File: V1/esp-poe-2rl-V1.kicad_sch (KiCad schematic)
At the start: 91 parts, among them J1 USB_C_Receptacle_USB2.0, J2 RJ45 JACK, J3 Conn_01x02, J4 Conn_01x02, K1 Relay 5V 15A, K2 Relay 5V 15A, Q1 WPM2015-3/TR, Q2 LMUN2211LT1G, Q3 UMH3N, Q4 MMBT2222A, Q5 MMBT2222A, SW1 RESET, U1 TPS2376D, U2 TX4138, U3 SY8089A1AAC, U4 CH340C, U5 ESP32-WROOM-32UE-N16, U6 LAN8710A

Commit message: Dev dev dev
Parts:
- J2: footprint Tales:RJ45_UDE_RB1-ZZ-0266 -> Tales:RJ45_UDE_RB1-ZZ-0206
- U1: value TPS2376D -> TPS2376DDAR-H
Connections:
- net +3.3VA: now also J2.12 (RLED+); no longer J2.L2 (RLED+)
- net LED_Y_A: now also J2.14 (LLED+); no longer J2.L4 (LLED+)
- net at R27.1: now also J2.13 (LLED-); no longer J2.L3 (LLED-)
- net at R28.1: now also J2.11 (RLED-); no longer J2.L1 (RLED-)
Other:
- note added: "OPÇÕES RJ45 UDE CORP RB1-ZZ-0266 JLCPCB C409617 HCTL HC931147C-M897-A JLCPCB C3021372 HANRUN HY931147C JLCPCB C91754 ABRACON ARJP11A-MASA-B-A-FMU2 MOUSER 815-ARJP11AMAFMU2 CUI DEVICES CRJ005-M1-TH MOUSER 490-CRJ005-M1-TH SEM LEDS SEM DIODOS MDD MB6S JLCPCB C2487 PONTE RETIFICADORA"
- note added: "R_{DIV1}"
- note added: "R_{DIV2}"
- note added: "V_{TAP} MUST BE 2.5V WHEN VDD IS AT THE DESIRED TURN ON VOLTAGE. V_{TAP} = V_{DD} * R_{DIV2} / (R_{DIV1}+R_{DIV2}) 2.5 = V_{DD} * 31.6 / 443.6 V_{DD} = 35.1V -> OK THE TOTAL RESISTANCE OF THE VOLTAGE DIVIDER WILL APPEAR IN PARALLEL WITH R_{DET} TO FORM THE EQUIVALENT RESISTANCE AT PIN DET. R_{EQUIV} = (R_{DIV1} + R_{DIV2}) // R_{DET} R_{EQUIV} = 443.6 // 26.7 R_{EQUIV} = 25.184k -> OK"
- note removed: "UDE CORP RB1-ZZ-0266 JLC C409617 1,24 ABRACON MOUSER 815-ARJP11AMAFMU2 9,05 CUI DEVICES MOUSER 490-CRJ005-M1-TH 5,67 NÃO TEM DIODOS INTERNOS JLCPCB C114100 MOLEX 424108312 JLCPCB C508567 JLCPCB C305935"
- note removed: "V_{TAP} MUST BE 2.5V WHEN VDD IS AT THE DESIRED TURN ON VOLTAGE. V_{TAP} = V_{DD} * R_{2} / (R_{1}+R_{2}) 2.5 = V_{DD} * 31.6 / 443.6 V_{DD} = 35.1V -> OK THE TOTAL RESISTANCE OF THE VOLTAGE DIVIDER (R_{1} + R_{2}) WILL APPEAR IN PARALLEL WITH R_{DET} TO FORM THE EQUIVALENT RESISTANCE AT PIN DET. R_{EQUIV} = (R_{1} + R_{2}) // R_{DET} R_{EQUIV} = 443.6 // 26.7 R_{EQUIV} = 25.184k -> OK"
- moved on the sheet: C2, R27, R28, R7

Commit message: dev goes on
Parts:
- R1: value 412k/62,5mW -> 130k/62,5mW; LCSC Part # C187991 -> C93946; Mfr TA-I Tech -> YAGEO; Mfr PN RM04FTN4123 -> RC0402FR-07130KL; Vendor PN C187991 -> C93946
- R13, R18, R19, R20, R21, R29, R32: LCSC Part # C25744 -> C60490; Mfr Uniroyal -> YAGEO; Mfr PN 0402WGF1002TCE -> RC0402FR-0710KL; Technology (none) -> 1%; Vendor PN C25744 -> C60490
- R2: value 31.6k/62,5mW -> 10k/62,5mW; LCSC Part # C100371 -> C60490; Mfr LIZ Elec -> YAGEO; Mfr PN CR0402FF3162G -> RC0402FR-0710KL; Vendor PN C100371 -> C60490
- R3: LCSC Part # C965284 -> C138046; Mfr Uniroyal -> YAGEO; Mfr PN NQ02WGF1803TCE -> RC0402FR-07180KL; Vendor PN C965284 -> C138046
- R4: value 4,42k/62,5mW -> 4,42k/100mW; footprint Tales:R_0402_1005Metric -> Tales:R_0603_1608Metric; Case 0402/1005 -> 0603/1608; LCSC Part # C173614 -> C482858; Mfr HKR -> YAGEO; Mfr PN RCT024K42FLF -> RC0603FR-074K42L; Vendor PN C173614 -> C482858
- R5: value 26,7k/62,5mW -> 30,1k/62,5mW; LCSC Part # C304992 -> C226982; Mfr Ralec -> YAGEO; Mfr PN RTT022672DTH -> AC0402FR-0730K1L; Technology 0,5% -> 1%; Vendor PN C304992 -> C226982
- R6: value 30mR/0,250W -> 30mR/250mW; LCSC Part # C247605 -> C859791; Mfr Uniroyal -> YAGEO; Mfr PN 0805W4F300MT5E -> RL0805FR-7W0R03L; Vendor PN C247605 -> C859791
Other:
- note added: "453/31.6 475/32.4 -> 26.1 178/12.1 -> 28.7"
- note added: "TPS2375 (IEEE 802.3af) TURN ON VOLTAGE = 39.3V TURN OFF VOLTAGE = 30.5V TPS2376-H TURN ON VOLTAGE: V_{TAP} = 2.49V HYSTERESIS = 0.56V TURN OFF VOLTAGE: V_{TAP} = 1.93V. V_{TAP} = V_{DD} * R_{DIV2} / (R_{DIV1}+R_{DIV2}) TURN ON: 2.5 = V_{DD} * 31.6 / 443.6 V_{DD} = 35.09V -> OK TURN 0FF: 1.93 = V_{DD} * 31.6 / 443.6 V_{DD} = 27.09V -> OK"
- note added: "VALUE FOR THE DETECTION RESISTANCE MUST BE 24.9K +/- 1% OR 24,651K TO 25.149K. THE TOTAL RESISTANCE OF THE VOLTAGE DIVIDER TO UVLO WILL APPEAR IN PARALLEL WITH R_{DET} TO FORM THE EQUIVALENT DETECTION RESISTANCE. R_{EQUIV} = (R_{DIV1} + R_{DIV2}) // R_{DET} R_{EQUIV} = 443.6 // 26.7 R_{EQUIV} = 25.184k -> OK"
- note removed: "V_{TAP} MUST BE 2.5V WHEN VDD IS AT THE DESIRED TURN ON VOLTAGE. V_{TAP} = V_{DD} * R_{DIV2} / (R_{DIV1}+R_{DIV2}) 2.5 = V_{DD} * 31.6 / 443.6 V_{DD} = 35.1V -> OK THE TOTAL RESISTANCE OF THE VOLTAGE DIVIDER WILL APPEAR IN PARALLEL WITH R_{DET} TO FORM THE EQUIVALENT RESISTANCE AT PIN DET. R_{EQUIV} = (R_{DIV1} + R_{DIV2}) // R_{DET} R_{EQUIV} = 443.6 // 26.7 R_{EQUIV} = 25.184k -> OK"

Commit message: Topology ok, checking components values
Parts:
- removed C1: 100nF/100V, Tales:C_1206_3216Metric, symbol Device:C_Small
- removed C10, C8, C9: 22uF/10V, symbol Device:C_Small
- removed C11: 10uF/10V, Tales:C_0603_1608Metric, symbol Device:C_Small
- removed C2: 15uF/100V, Capacitor_SMD:CP_Elec_8x6.2, symbol Device:C_Polarized_Small_US
- removed C3: 0,1uF/50V, Tales:C_0805_2012Metric, symbol Device:C_Small
- removed C4: 12pF/50V, Tales:C_0603_1608Metric, symbol Device:C_Small
- removed C5: 470uF/16V, Tales:CP_Elec_10x10, symbol Device:C_Polarized_Small_US
- removed C6: 10uF/10V, symbol Device:C_Small
- removed C7: 22pF/10V, symbol Device:C_Small
- removed D1: SMAJ58A, Tales:D_SMA, symbol Device:D_Zener_Small
- removed D2: SS510, Tales:D_SMA, symbol Device:D_Schottky_Small
- removed D3: SS34, Tales:D_SMA, symbol Device:D_Schottky_Small
- removed D4: B5819W, Tales:D_SOD-123, symbol Device:D_Schottky_Small
- removed D5: GREEN, Tales:LED_0603_1608Metric, symbol Device:LED_Small
- removed K1, K2: Relay 5V 15A, symbol Tales:G5PZ-1A
- removed L1: 33uH/2,1A, Tales:L_12x12mm_H6mm, symbol Device:L
- removed L2: 2,2uH/1,5A, Tales:L_3x3_H1.5, symbol Device:L
- removed Q1: WPM2015-3/TR, Tales:SOT-23, symbol Device:Q_PMOS_GSD
- removed Q2: LMUN2211LT1G, Tales:SOT-23, symbol Device:Q_NPN_BEC_BRT
- removed R1: 130k/62,5mW, Tales:R_0402_1005Metric, symbol Device:R_US
- removed R10: 52,3k/0,125W, Tales:R_0805_2012Metric, symbol Device:R_US
- removed R11: 100k/0,125W, Tales:R_0805_2012Metric, symbol Device:R_US
- removed R12: 22,1k/0,125W, Tales:R_0805_2012Metric, symbol Device:R_US
- removed R13, R2, R32: 10k/62,5mW, Tales:R_0402_1005Metric, symbol Device:R_US
- removed R14, R33: 1k/62,5mW, Tales:R_0402_1005Metric, symbol Device:R_US
- removed R17, R31, R34: 820R/62,5mW, Tales:R_0402_1005Metric, symbol Device:R_US
- removed R3: 180k/62,5mW, Tales:R_0402_1005Metric, symbol Device:R_US
- removed R4: 4,42k/100mW, Tales:R_0603_1608Metric, symbol Device:R_US
- removed R5: 30,1k/62,5mW, Tales:R_0402_1005Metric, symbol Device:R_US
- removed R6: 30mR/250mW, Tales:R_0805_2012Metric, symbol Device:R_US
- removed R7: 4,7k/1W, Tales:R_2512_6332Metric, symbol Device:R_US
- removed R8: 5,1R/0,125W, Tales:R_0805_2012Metric, symbol Device:R_US
- removed R9: 300k/0,125W, Tales:R_0805_2012Metric, symbol Device:R_US
- removed U1: TPS2376DDAR-H, Package_SO:SOIC-8-1EP_3.9x4.9mm_P1.27mm_EP2.95x4.9mm_Mask2.71x3.4mm_ThermalVias, symbol Tales:TPS2376
- removed U2: TX4138, Tales:SOIC-8-1EP_3.9x4.9mm_P1.27mm_EP2.29x3mm_ThermalVias, symbol Tales:TX4138
- removed U3: SY8089A1AAC, Tales:TSOT-23-5, symbol Tales:SY8089AAAC
- added C24: 22uF/10V, Tales:C_1206_3216Metric, symbol Device:C_Small
- added C25: 10uF/10V, Tales:C_0603_1608Metric, symbol Device:C_Small
- added K1, K2: Songle SRD-5VDC-SL-A, Tales:Relay_SPST_Songle_SRD_FormA, symbol Tales:Songle_SRD
- added Q2: WPM2015-3/TR, Tales:SOT-23, symbol Device:Q_PMOS_GSD
- added Q3: LMUN2211LT1G, Tales:SOT-23, symbol Device:Q_NPN_BEC_BRT
- added R27: 820R/62,5mW, Tales:R_0402_1005Metric, symbol Device:R_US
- added R28: 10k/62,5mW, Tales:R_0402_1005Metric, symbol Device:R_US
- added RN3: 4x49,9R/62,5mW, Resistor_SMD:R_Array_Convex_4x0402, symbol Device:R_Pack04
- J3, J4: footprint (none) -> Tales:TerminalBlock_JL142V-5.08-2P_1x02_P5.08mm_Vertical; JLCPCB BOM (none) -> 1; LCSC Part # (none) -> C409160; Mfr (none) -> JILN; Mfr PN (none) -> JL142V-50802GA1; Vendor (none) -> JLCPCB; Vendor PN (none) -> C409160
- R14: renamed from R15; LCSC Part # C319557 -> C105872; Mfr Viking Tech -> YAGEO; Mfr PN AR02DTD5101 -> RC0402FR-075K1L; Vendor PN C319557 -> C105872
- R15: renamed from R16; LCSC Part # C319557 -> C105872; Mfr Viking Tech -> YAGEO; Mfr PN AR02DTD5101 -> RC0402FR-075K1L; Vendor PN C319557 -> C105872
- R23, R25: value 49,9R/62,5mW -> 10k/62,5mW; LCSC Part # C25120 -> C60490; Mfr Uniroyal -> YAGEO; Mfr PN 0402WGF499JTCE -> RC0402FR-0710KL; Technology (none) -> 1%; Vendor PN C25120 -> C60490
- R24, R26: value 49,9R/62,5mW -> 1k/62,5mW; LCSC Part # C25120 -> C11702; Mfr PN 0402WGF499JTCE -> 0402WGF1001TCE; Vendor PN C25120 -> C11702
- R29: value 10k/62,5mW -> 1k/62,5mW; LCSC Part # C60490 -> C11702; Mfr YAGEO -> Uniroyal; Mfr PN RC0402FR-0710KL -> 0402WGF1001TCE; Technology 1% -> (none); Vendor PN C60490 -> C11702
- R30: value 1k/62,5mW -> 820R/62,5mW; LCSC Part # C11702 -> C423266; Mfr PN 0402WGF1001TCE -> 0402WGD8200TCE; Vendor PN C11702 -> C423266
- RN1, RN2: footprint (none) -> Resistor_SMD:R_Array_Convex_4x0402; Case (none) -> 4x0402; LCSC Part # C458647 -> C414595; Mfr RALEC -> Uniroyal; Mfr PN RTA02-4D222JTH -> 4D02WGF2201TCE; Vendor PN C458647 -> C414595
- renumbered C12 to C10, C13 to C11, C14 to C12, C15 to C13, C16 to C14, C17 to C15, C18 to C16, C19 to C17, C20 to C18, C21 to C19, C22 to C20, C23 to C21, C24 to C22, C25 to C23, Q3 to Q1, R18 to R16, R19 to R17, R20 to R18, R21 to R19, R22 to R20, R28 to R21, R27 to R22
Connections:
- net +3.3V: now also R23.1, C24.1, Q2.2 (S)
- net +3.3VA: now also RN3.5 (R4.2), RN3.6 (R3.2), RN3.7 (R2.2), RN3.8 (R1.2); no longer R23.2, R24.2, R25.2, R26.2
- net +3.3VLAN: now also R19.2, C25.1, Q2.3 (D); no longer R19.1
- net +5V: now also R30.1, K1.A1, K2.A1, R27.1; no longer F1.1
- net GND: now also C15.1, R18.1, R25.2, C25.2, Q3.2 (E), R28.2; no longer C15.2, R18.2, R29.2
- net OUT1: now also R25.1, R26.2; no longer R29.1, R30.2
- net OUT2: now also R29.2, R28.1
- net PHY_PWR: now also R18.2, Q3.1 (B); no longer R18.1
- net RD+: now also RN3.3 (R3.1); no longer R25.1
- net RD-: now also RN3.4 (R4.1); no longer R26.1
- net TD+: now also RN3.1 (R1.1); no longer R23.1
- net TD-: now also RN3.2 (R2.1); no longer R24.1
- net at D8.1 (K), Q5.3 (C): now also K2.A2
- net at J4.2 (Pin_2): now also K2.11
- net at J4.1 (Pin_1): now also K2.14
- net at Q5.1 (B): now also R29.1
- net at F1.2: now also C10.1, C11.1, J1.A4 (VBUS), J1.A9 (VBUS), J1.B4 (VBUS), J1.B9 (VBUS)
- net at Q4.1 (B): now also R26.1; no longer R30.1
- net at J3.1 (Pin_1): now also K1.14
- net at J3.2 (Pin_2): now also K1.11
- net at D7.2 (A): now also R27.2
- net at D7.1 (K), Q4.3 (C): now also K1.A2
- net at D8.2 (A): now also R30.2
- new net: C15.2, R19.1, U6.19 (~{RST})
- new net: C24.2, Q2.1 (G), R23.2, R24.1
- new net: Q3.3 (C), R24.2
- new net 5VUSB: F1.1
- no-connect marks 30 -> 29
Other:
- added sheet POWER (esp-poe-2rl-V1-power.kicad_sch)
- note added: "ESP32 TEMPLATE FOR GPIO ASSIGNMENT {"NAME":"ESP-24V-16CH-V2","GPIO":[1,3200,0,3232,0,0,0,0, 5536,10240,10241,0,0,0,5600,0,0,0,0,5568,0,0,0,0,0,0,0,0, 608,640,0,0,0,0,0,0],"FLAG":0,"BASE":1} https://tasmota.github.io/docs/Templates/"
- note added: "OPÇÕES DE CONECTORES RJ45 UDE CORP RB1-ZZ-0266 JLCPCB C409617 HCTL HC931147C-M897-A JLCPCB C3021372 HANRUN HY931147C JLCPCB C91754 ABRACON ARJP11A-MASA-B-A-FMU2 MOUSER 815-ARJP11AMAFMU2 CUI DEVICES CRJ005-M1-TH MOUSER 490-CRJ005-M1-TH SEM LEDS SEM DIODOS MDD MB6S JLCPCB C2487 PONTE RETIFICADORA"
- note removed: "453/31.6 475/32.4 -> 26.1 178/12.1 -> 28.7"
- note removed: "OPÇÕES RJ45 UDE CORP RB1-ZZ-0266 JLCPCB C409617 HCTL HC931147C-M897-A JLCPCB C3021372 HANRUN HY931147C JLCPCB C91754 ABRACON ARJP11A-MASA-B-A-FMU2 MOUSER 815-ARJP11AMAFMU2 CUI DEVICES CRJ005-M1-TH MOUSER 490-CRJ005-M1-TH SEM LEDS SEM DIODOS MDD MB6S JLCPCB C2487 PONTE RETIFICADORA"
- note removed: "R_{1}"
- note removed: "R_{1} = (V_{OUT} - 0,6V) * R_{2} / 0,6V V_{OUT} = (0,6 * R_{1} / R_{2}) + 0,6 V_{OUT} = (0,6 * 100k/22,1k) +0,6 V_{OUT} = 3,31V"
- note removed: "R_{2}"
- note removed: "R_{2} = R_{1}/(V_{OUT} / 0,805 - 1) V_{OUT} = (R_{1} / R_{2}) + 1) * 0,805 V_{OUT} = (300k / 52,3k + 1) * 0,805 V_{OUT} = 5,42V VOLTAGE DROP AT DIODE SS34 @2A = 0,4V 5V MAIN BUS @2A = 5,02V"
- note removed: "R_{CLASS}"
- note removed: "R_{CLASS} = 4420R 1% CLASS 0 0.44 - 12,95W"
- note removed: "R_{DET}"
- note removed: "R_{DIV1}"
- note removed: "R_{DIV2}"
- note removed: "TEMPLATE FOR GPIO ASSIGNMENT {"NAME":"ESP-24V-16CH-V2","GPIO":[1,3200,0,3232,0,0,0,0,5536,10240,10241,0,0, 0,5600,0,0,0,0,5568,0,0,0,0,0,0,0,0,608,640,0,0,0,0,0,0],"FLAG":0,"BASE":1} https://tasmota.github.io/docs/Templates/"
- note removed: "TEMPLATE FOR MCP23017 I/O ASSIGNMENT {"NAME":"MCP23017 expander","BASE":0,"GPIO":[160,161,162,163,164,165,166,167,168,169,170, 171,172,173,174,175,224,225,226,227,228,229,230,231,232,233,234,235,236,237,238,239]} https://tasmota.github.io/docs/MCP230xx/"
- note removed: "TPS2375 (IEEE 802.3af) TURN ON VOLTAGE = 39.3V TURN OFF VOLTAGE = 30.5V TPS2376-H TURN ON VOLTAGE: V_{TAP} = 2.49V HYSTERESIS = 0.56V TURN OFF VOLTAGE: V_{TAP} = 1.93V. V_{TAP} = V_{DD} * R_{DIV2} / (R_{DIV1}+R_{DIV2}) TURN ON: 2.5 = V_{DD} * 31.6 / 443.6 V_{DD} = 35.09V -> OK TURN 0FF: 1.93 = V_{DD} * 31.6 / 443.6 V_{DD} = 27.09V -> OK"
- note removed: "USB 2.0 -> 5V 500mA USB 3.0 -> 5V 900mA VOLTAGE DROP AT DIODE B5819W @500mA = 0,4V 5V USB BUS @500mA = 4,6V"
- note removed: "VALUE FOR THE DETECTION RESISTANCE MUST BE 24.9K +/- 1% OR 24,651K TO 25.149K. THE TOTAL RESISTANCE OF THE VOLTAGE DIVIDER TO UVLO WILL APPEAR IN PARALLEL WITH R_{DET} TO FORM THE EQUIVALENT DETECTION RESISTANCE. R_{EQUIV} = (R_{DIV1} + R_{DIV2}) // R_{DET} R_{EQUIV} = 443.6 // 26.7 R_{EQUIV} = 25.184k -> OK"
- note removed: "V_{TAP}"
- moved on the sheet: C10, C11, C12, C13, C14, C15, C16, C17, C18, C19, C20, C21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

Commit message: Revising components specs
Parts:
- D6: footprint Package_TO_SOT_SMD:SOT-23-5 -> Tales:SOT-23-5
- F1: footprint Fuse:Fuse_1206_3216Metric -> Tales:Fuse_1206_3216Metric
- L3: footprint Inductor_SMD:L_0805_2012Metric -> Tales:L_0805_2012Metric
- RN1, RN2, RN3: footprint Resistor_SMD:R_Array_Convex_4x0402 -> Tales:R_Array_Convex_4x0402
- SW1: footprint Button_Switch_SMD:SW_SPST_TL3342 -> Tales:SW_SPST_TL3342
- U4: footprint Package_SO:SOIC-16_3.9x9.9mm_P1.27mm -> Tales:SOIC-16_3.9x9.9mm_P1.27mm
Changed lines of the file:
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@@
       (effects (font (size 1.27 1.27)))
     )
-    (property "Footprint" "Package_TO_SOT_SMD:SOT-23-5" (at 378.46 110.49 0)
+    (property "Footprint" "Tales:SOT-23-5" (at 378.46 110.49 0)
       (effects (font (size 1.27 1.27)) hide)
     )
@@
       (effects (font (size 1.27 1.27)))
     )
-    (property "Footprint" "Fuse:Fuse_1206_3216Metric" (at 64.77 34.29 0)
+    (property "Footprint" "Tales:Fuse_1206_3216Metric" (at 64.77 34.29 0)
       (effects (font (size 1.27 1.27)) hide)
     )
@@
       (effects (font (size 1.27 1.27)) (justify right))
     )
-    (property "Footprint" "Resistor_SMD:R_Array_Convex_4x0402" (at 259.715 54.61 90)
+    (property "Footprint" "Tales:R_Array_Convex_4x0402" (at 259.715 54.61 90)
       (effects (font (size 1.27 1.27)) hide)
     )
@@
       (effects (font (size 1.27 1.27)))
     )
-    (property "Footprint" "Resistor_SMD:R_Array_Convex_4x0402" (at 377.19 151.765 90)
+    (property "Footprint" "Tales:R_Array_Convex_4x0402" (at 377.19 151.765 90)
       (effects (font (size 1.27 1.27)) hide)
     )
@@
       (effects (font (size 1.27 1.27)) (justify left))
     )
-    (property "Footprint" "Resistor_SMD:R_Array_Convex_4x0402" (at 272.415 54.61 90)
+    (property "Footprint" "Tales:R_Array_Convex_4x0402" (at 272.415 54.61 90)
       (effects (font (size 1.27 1.27)) hide)
     )
@@
       (effects (font (size 1.27 1.27)) (justify right))
     )
-    (property "Footprint" "Package_SO:SOIC-16_3.9x9.9mm_P1.27mm" (at 100.33 82.55 0)
+    (property "Footprint" "Tales:SOIC-16_3.9x9.9mm_P1.27mm" (at 100.33 82.55 0)
       (effects (font (size 1.27 1.27)) (justify left) hide)
     )
@@
       (effects (font (size 1.27 1.27)))
     )
-    (property "Footprint" "Inductor_SMD:L_0805_2012Metric" (at 90.17 163.83 0)
+    (property "Footprint" "Tales:L_0805_2012Metric" (at 90.17 163.83 0)
       (effects (font (size 1.27 1.27)) hide)
     )
@@
       (effects (font (size 1.27 1.27)) (justify right))
     )
-    (property "Footprint" "Button_Switch_SMD:SW_SPST_TL3342" (at 137.16 107.95 0)
+    (property "Footprint" "Tales:SW_SPST_TL3342" (at 137.16 107.95 0)
       (effects (font (size 1.27 1.27)) hide)
     )

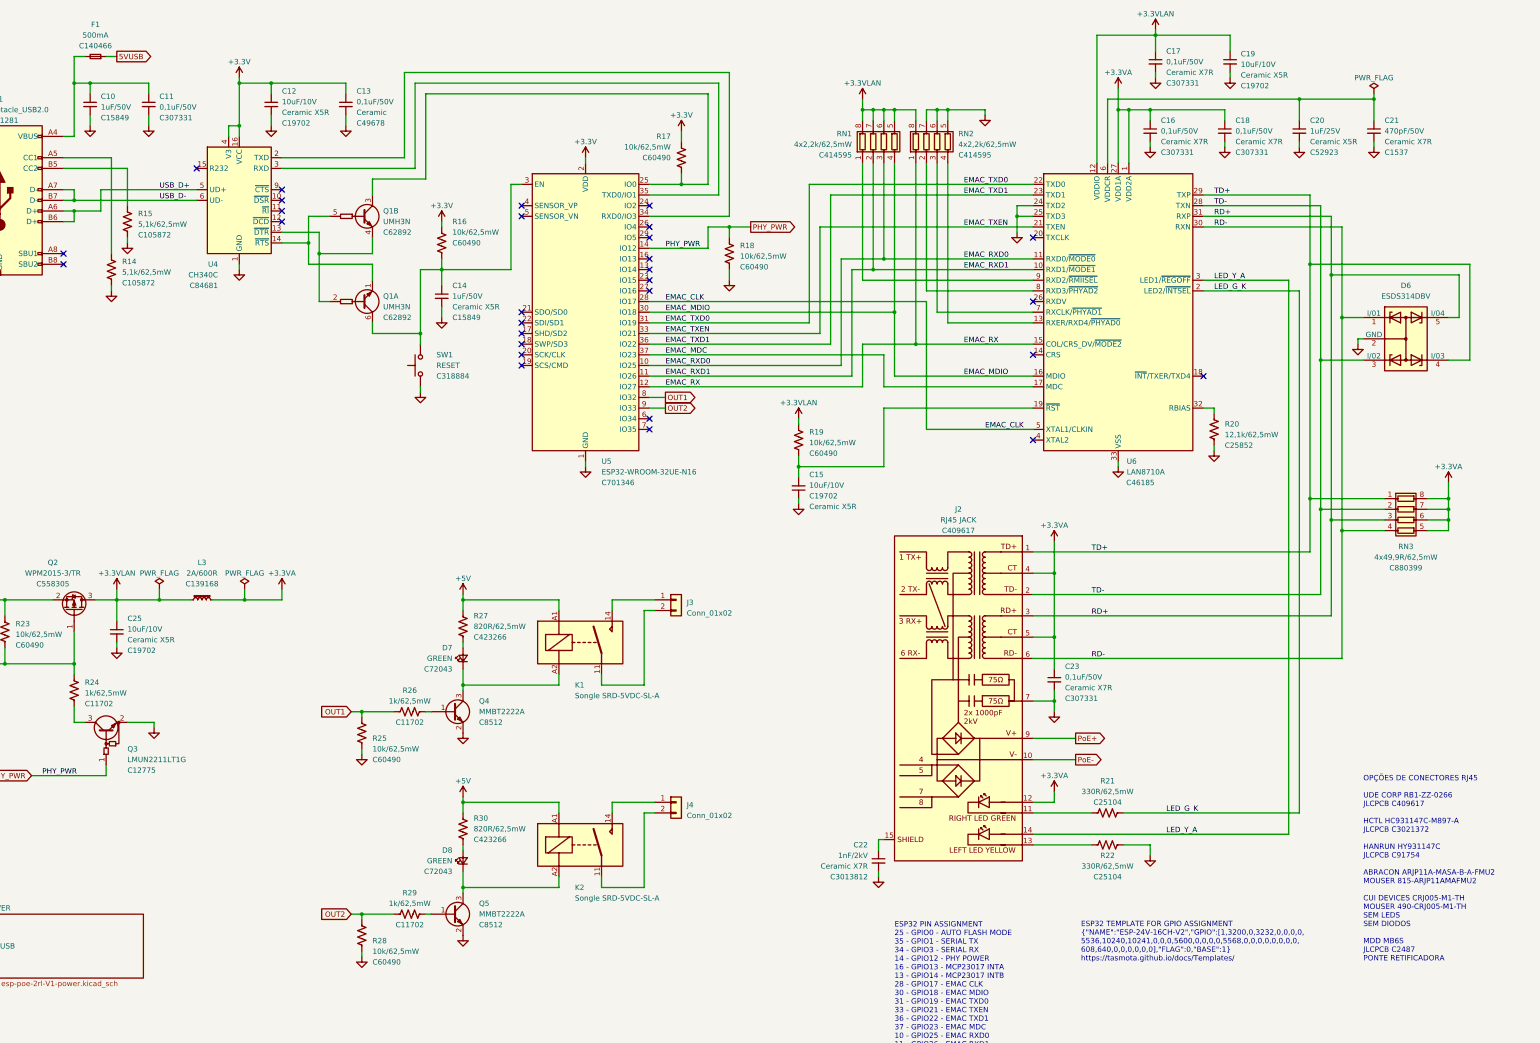
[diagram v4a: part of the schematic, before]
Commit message: Reviewing components
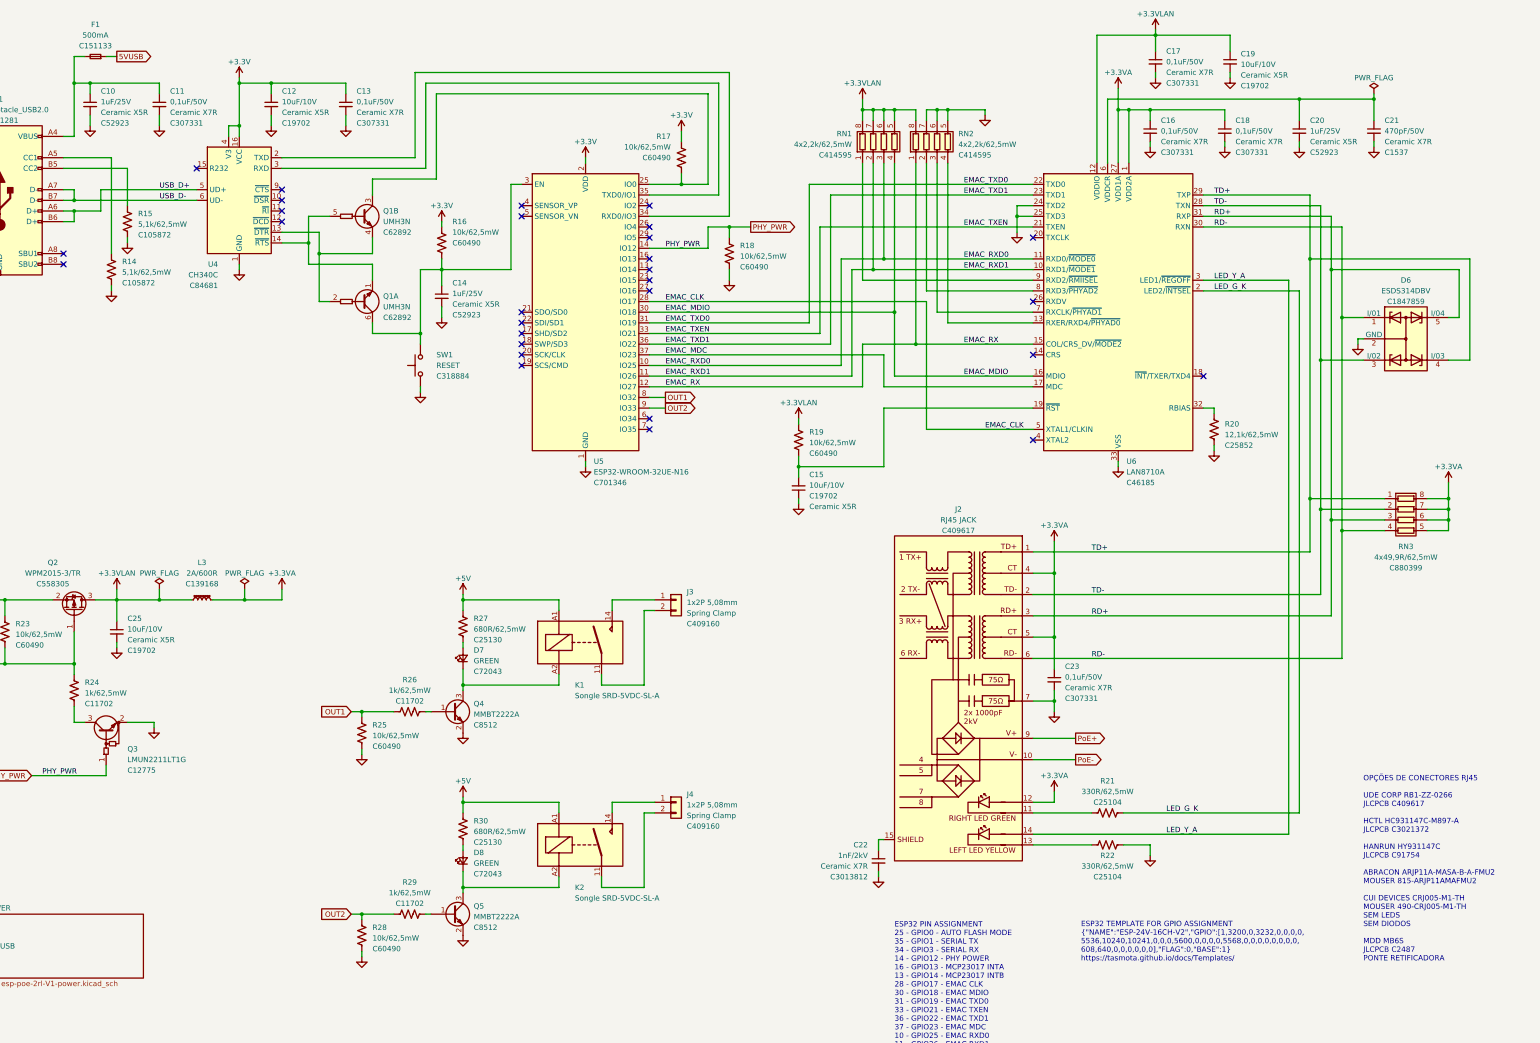
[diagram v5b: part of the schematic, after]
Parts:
- C10, C14: value 1uF/50V -> 1uF/25V; footprint Tales:C_0603_1608Metric -> Tales:C_0402_1005Metric; Case 0603/1608 -> 0402/1005; LCSC Part # C15849 -> C52923; Mfr PN CL10A105KB8NNNC -> CL05A105KA5NQNC; Vendor PN C15849 -> C52923
- C13: footprint Tales:C_0805_2012Metric -> Tales:C_0402_1005Metric; Case 0805/2012 -> 0402/1005; LCSC Part # C49678 -> C307331; Mfr Yageo -> Samsung; Mfr PN CC0805KRX7R9BB104 -> CL05B104KB54PNC; Technology Ceramic -> Ceramic X7R; Vendor PN C49678 -> C307331
- D7, D8: Technology (none) -> InGaN
- F1: LCSC Part # C140466 -> C151133; Mfr Xucheng Elec -> Littlefuse; Mfr PN 12F.05000063AG12S1B02 -> 0466.500NRHF; Vendor PN C140466 -> C151133
- J3, J4: value Conn_01x02 -> 1x2P 5,08mm; Technology (none) -> Spring Clamp
- K1, K2: Case (none) -> SPST Form A
- R14, R15, R20, R21, R22, R24, R26, R29, RN1, RN2, RN3: Technology (none) -> 1%
- R16, R17, R18, R19, R23, R25, R28: Mfr YAGEO -> Yageo
- R27, R30: value 820R/62,5mW -> 680R/62,5mW; LCSC Part # C423266 -> C25130; Mfr PN 0402WGD8200TCE -> 0402WGF6800TCE; Technology (none) -> 1%; Vendor PN C423266 -> C25130
- SW1: Case (none) -> SPST; Technology (none) -> Tactile
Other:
- moved on the sheet: C11

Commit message: Starting layout
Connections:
- net EMAC_MDIO: now also RN1.1 (R1.1); no longer RN1.4 (R4.1)
- net EMAC_RX: now also RN1.2 (R2.1); no longer RN2.1 (R1.1)
- net EMAC_RXD1: now also RN1.4 (R4.1); no longer RN1.2 (R2.1)
- net RD+: now also RN3.1 (R1.1); no longer RN3.3 (R3.1)
- net RD-: now also RN3.2 (R2.1); no longer RN3.4 (R4.1)
- net TD+: now also RN3.3 (R3.1); no longer RN3.1 (R1.1)
- net TD-: now also RN3.4 (R4.1); no longer RN3.2 (R2.1)
- net at U6.9 (RXD2/~{RMIISEL}): now also RN2.1 (R1.1); no longer RN1.1 (R1.1)

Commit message: Layout development
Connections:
- net +3.3VLAN: now also RN2.7 (R2.2); no longer RN1.6 (R3.2)
- net EMAC_RXD0: now also RN1.4 (R4.1); no longer RN1.3 (R3.1)
- net EMAC_RXD1: now also RN2.1 (R1.1); no longer RN1.4 (R4.1)
- net GND: now also RN1.6 (R3.2); no longer RN2.7 (R2.2)
- net TD+: now also RN3.4 (R4.1); no longer RN3.3 (R3.1)
- net TD-: now also RN3.3 (R3.1); no longer RN3.4 (R4.1)
- net at U6.13 (RXER/RXD4/~{PHYAD0}): now also RN1.3 (R3.1); no longer RN2.4 (R4.1)
- net at U6.7 (RXCLK/~{PHYAD1}): now also RN2.4 (R4.1); no longer RN2.3 (R3.1)
- net at U6.8 (RXD3/~{PHYAD2}): now also RN2.3 (R3.1); no longer RN2.2 (R2.1)
- net at U6.9 (RXD2/~{RMIISEL}): now also RN2.2 (R2.1); no longer RN2.1 (R1.1)
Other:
- moved on the sheet: C15, R19

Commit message: PCB design
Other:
- note added: "SUBSTITUIR POR C2765186"
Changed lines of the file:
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@@
+    (effects (font (size 1.27 1.27)) (justify left bottom))
+  )
+  (text "SUBSTITUIR POR C2765186" (at 29.21 101.6 0)
     (effects (font (size 1.27 1.27)) (justify left bottom))
   )
